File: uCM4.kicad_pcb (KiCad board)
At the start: 2 copper layers, 55 x 40 mm, 39 parts, among them J1 Conn_01x03, J2 Ethernet, J3 Micro_SD_Card, J4 USB_B_Micro, SW1 SW_DIP_x01, SW2 SW_DIP_x01, U1 RT9742GGJ5, U2 74LVC1G07, U3 TPD4EUSB30

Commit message: Bump to version 0.2.0
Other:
- board text added: "µCM4-Net v0.2.0"
- board text removed: "µCM4-Net v0.1.1"
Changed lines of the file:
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@@
   (gr_line (start 175.94 85.04) (end 120.94 125.04) (layer "User.2") (width 0.15))
   (gr_line (start 120.94 88.55) (end 120.94 84.38) (layer "User.2") (width 0.15))
-  (gr_text "µCM4-Net v0.1.1" (at 126.5 111.5 270) (layer "B.SilkS")
+  (gr_text "µCM4-Net v0.2.0" (at 126.5 111.5 270) (layer "B.SilkS")
     (effects (font (size 1 1) (thickness 0.15)) (justify mirror))
   )

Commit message: Add TODOs for planned changes in PCB layout
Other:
- board text added: "TODO: LEDs here"
- board text added: "TODO: SOT-23-5"
- board text added: "TODO: btn here"
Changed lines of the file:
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@@
     (effects (font (size 1 1) (thickness 0.15)))
+  )
+  (gr_text "TODO: LEDs here" (at 172.37 117.11) (layer "User.4")
+    (effects (font (size 0.5 0.5) (thickness 0.125)))
+  )
+  (gr_text "TODO: SOT-23-5" (at 158.71 91.8) (layer "User.4")
+    (effects (font (size 0.5 0.5) (thickness 0.125)))
+  )
+  (gr_text "TODO: btn here" (at 172.55 94.2) (layer "User.4")
+    (effects (font (size 0.5 0.5) (thickness 0.125)))
   )
   (segment (start 139.777771 104.500012) (end 145.620012 104.500012) (width 0.13) (layer "F.Cu") (net 3))

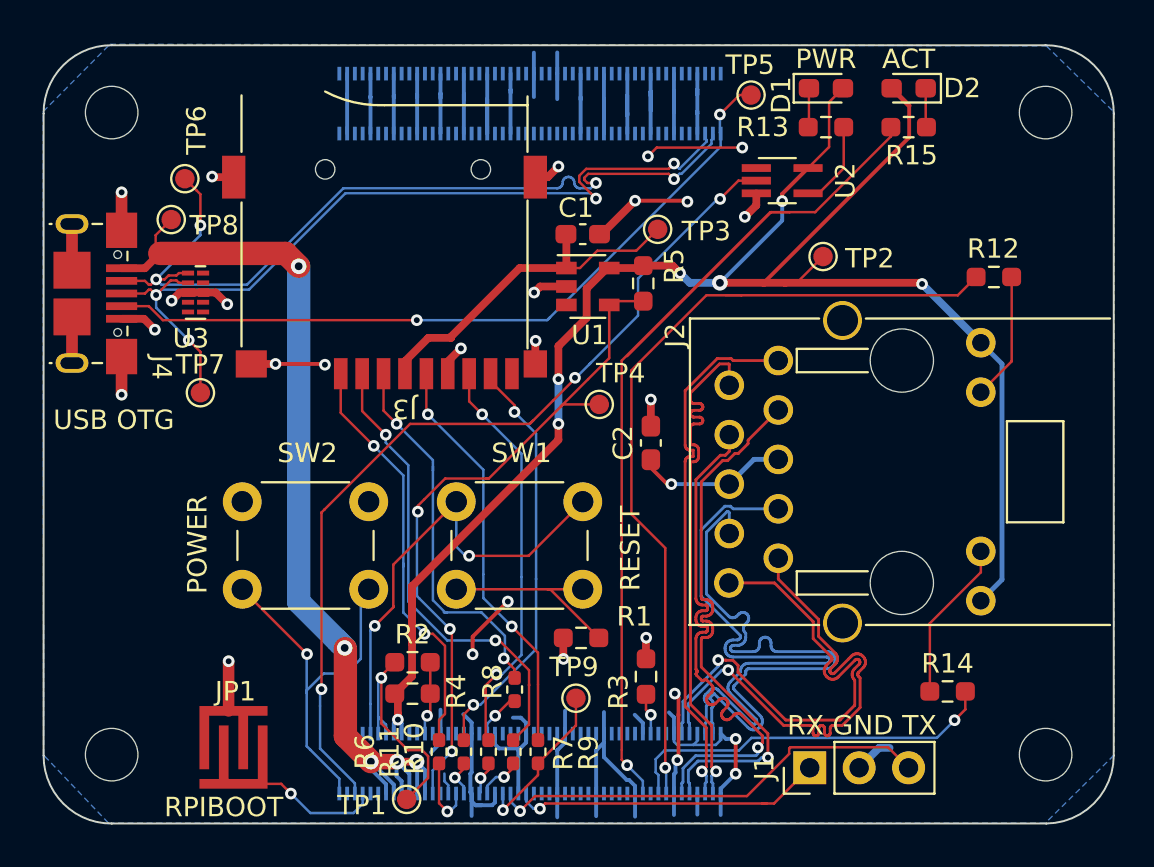
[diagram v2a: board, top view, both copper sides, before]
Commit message: Make preparations for required changes in 0.2.0
Following has been performed and could not be made separately:
- move LEDs to smaller space next to Ethernet
- move buttons to bigger space next to Ethernet
- two changes above makes together handy interface for whole board,
  where almost everything needed is on one side
- move all parts belonging to LEDs and buttons near their new locations
- change footprint of buffer chip to SOT-23-5, which is more likely to
  be used in this version
- reroute traces for all moved parts and do some small adjustments in
  other traces for easier routing (buttons not completed yet!)
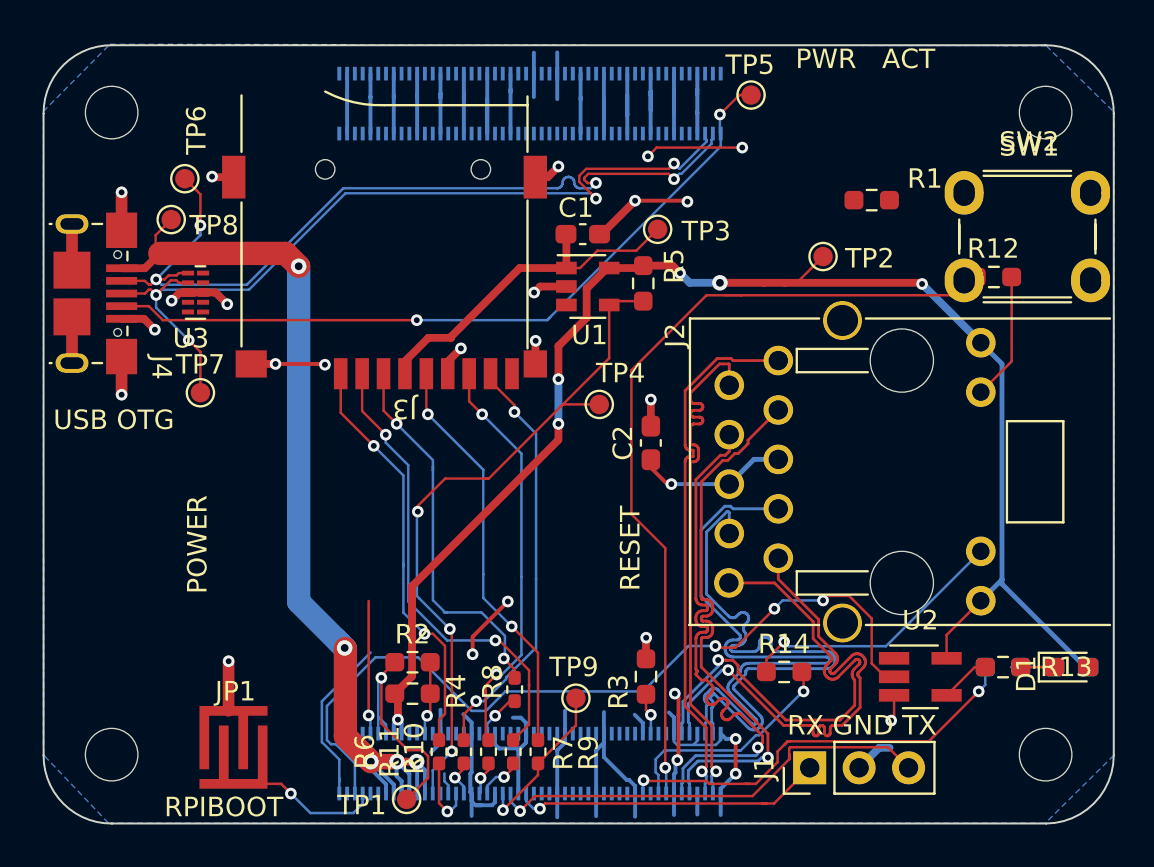
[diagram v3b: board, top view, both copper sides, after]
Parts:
- D2, R15: moved to B.Cu
- U2: footprint Package_TO_SOT_SMD:SOT-353_SC-70-5_Handsoldering -> Package_TO_SOT_SMD:SOT-23-5_HandSoldering
- moved SW2 40.4 mm to (168.2, 92.5)
- moved D1 32.3 mm to (173.8, 117.0)
- moved D2 30.9 mm to (173.8, 117.0), turned to 0 degrees
- moved SW1 30.5 mm to (174.8, 97.2)
- moved R13 29.2 mm to (170.2, 117.0), turned to 0 degrees
- moved R15 28.2 mm to (170.2, 117.0)
- moved R1 27.0 mm to (163.5, 93.0)
- moved U2 26.5 mm to (166.0, 117.5)
- moved R14 8.46 mm to (159.0, 117.2)
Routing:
- net Net-(Module1-Pad21): track 53.2 -> 22.3 mm, vias 1 -> 2
- net /RESET: track 23.9 -> 6.86 mm, vias 2 -> 1
- net +3V3: track 96.3 -> 80.4 mm, vias 7 -> 6
- net /PowerOn: track 19.9 -> 8.78 mm, vias 1 -> 0
- net Net-(R1-Pad1): track 10.2 -> 0.00 mm
- net Net-(Module1-Pad17): track 19.7 -> 11.9 mm
- net Net-(J2-PadL3): track 8.29 -> 14.2 mm, vias 0 -> 1
- net /nPWR_LED: track 46.1 -> 41.9 mm
- net /nPWR_LED_Buffered: track 4.48 -> 2.59 mm
- net GND: track 160.3 -> 159.2 mm, vias 27 -> 26

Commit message: Remove TODOs
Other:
- board text removed: "TODO: LEDs here"
- board text removed: "TODO: SOT-23-5"
- board text removed: "TODO: btn here"
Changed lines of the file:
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@@
     (effects (font (size 1 1) (thickness 0.15)))
-  )
-  (gr_text "TODO: LEDs here" (at 172.37 117.11) (layer "User.4")
-    (effects (font (size 0.5 0.5) (thickness 0.125)))
-  )
-  (gr_text "TODO: SOT-23-5" (at 165.25 117.5) (layer "User.4")
-    (effects (font (size 0.5 0.5) (thickness 0.125)))
-  )
-  (gr_text "TODO: btn here" (at 172.55 94.2) (layer "User.4")
-    (effects (font (size 0.5 0.5) (thickness 0.125)))
   )
   (segment (start 164.195 117.5) (end 163.5 116.805) (width 0.13) (layer "F.Cu") (net 3))

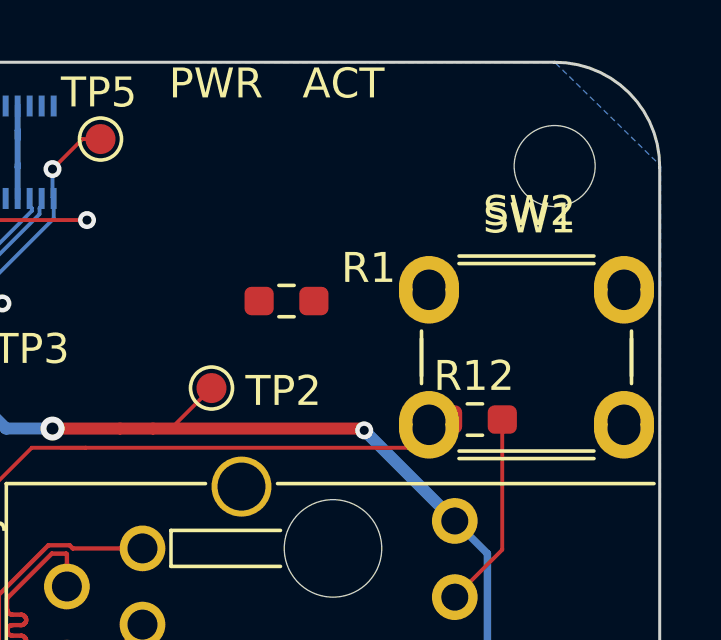
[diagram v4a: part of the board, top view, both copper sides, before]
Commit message: Update footprint for buttons
Now should point to almost finished PTS840.
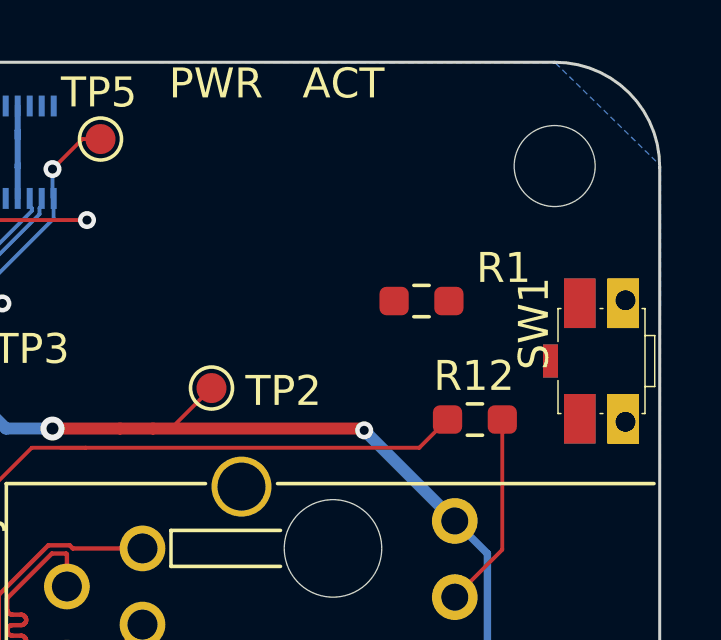
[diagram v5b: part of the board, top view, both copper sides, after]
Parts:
- SW1: footprint Button_Switch_THT:SW_PUSH_6mm -> KiCAD_Randoms:PTS840_PM_SMTR_LFS
- SW2: footprint Button_Switch_THT:SW_PUSH_6mm -> KiCAD_Randoms:PTS840_PM_SMTR_LFS; moved to B.Cu
- moved SW2 6.27 mm to (174.0, 95.0), turned to -90 degrees
- moved R1 4.50 mm to (168.0, 93.0)
- moved SW1 2.37 mm to (174.0, 95.0), turned to 90 degrees

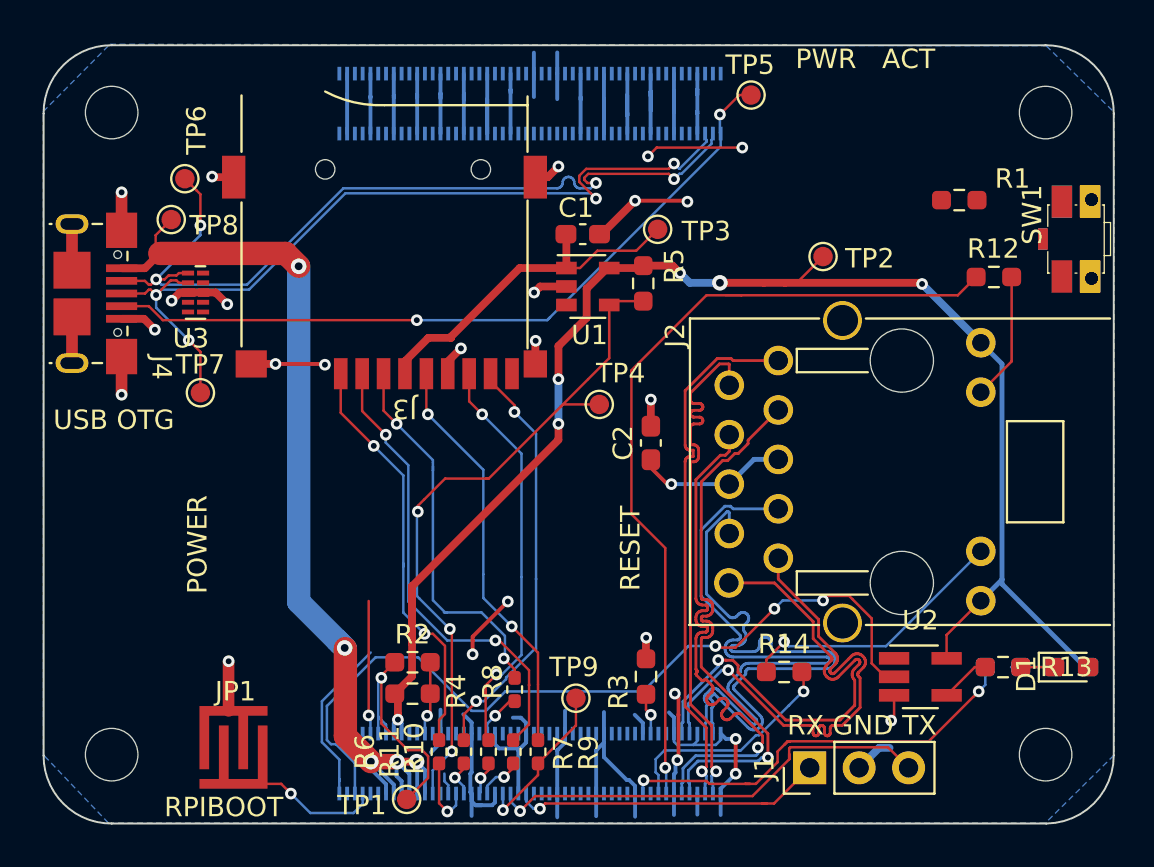
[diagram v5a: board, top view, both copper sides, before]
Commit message: Power buttons - issue #7
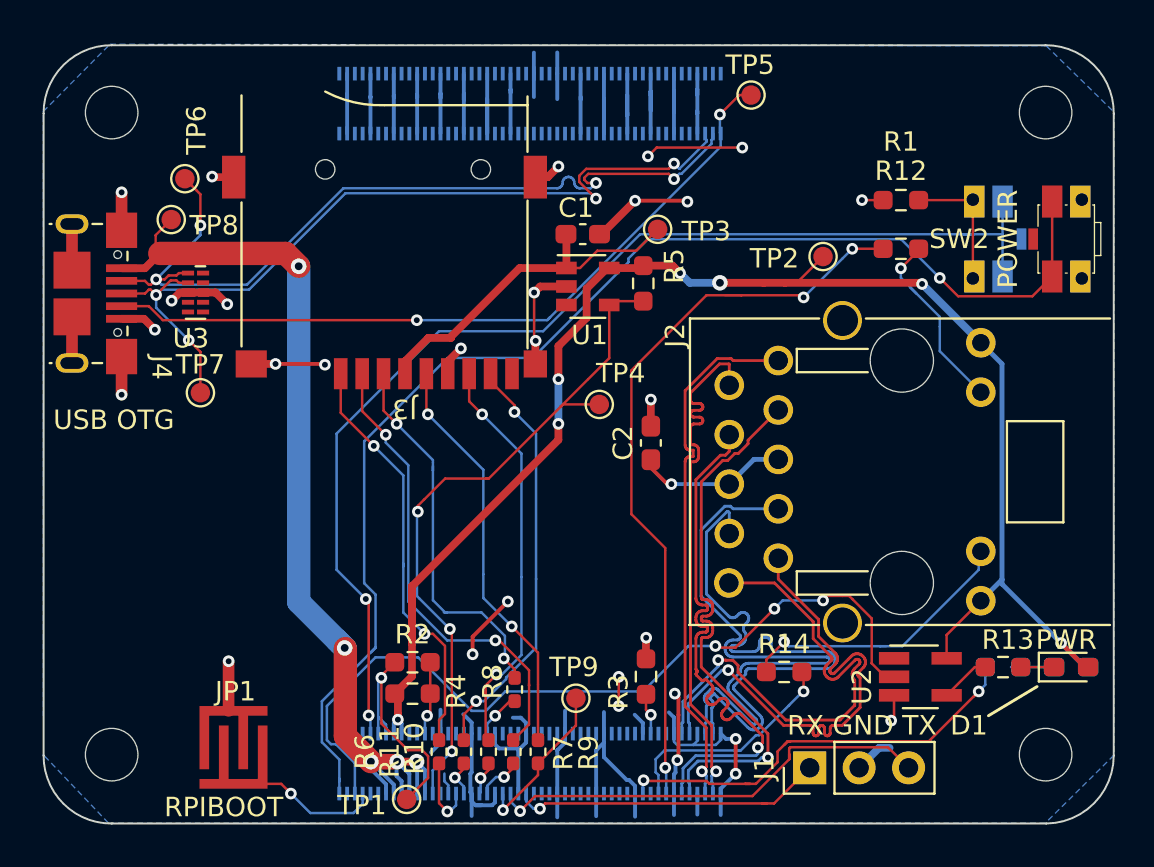
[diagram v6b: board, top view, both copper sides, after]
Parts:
- SW1: moved to B.Cu
- SW2: moved to F.Cu
- moved R12 5.00 mm to (165.0, 95.5)
- moved SW1 4.50 mm to (169.5, 95.0)
- moved R1 3.00 mm to (165.0, 93.0)
- moved SW2 0.50 mm to (173.5, 95.0), turned to 90 degrees
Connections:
- net Net-(Module1-Pad21) renamed /ACT_LED
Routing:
- net /PowerOn: track 8.78 -> 65.7 mm, vias 0 -> 1
- net /RESET: track 6.86 -> 59.0 mm, vias 1 -> 2
- net Net-(R1-Pad1): track 0.00 -> 6.85 mm
- net GND: track 159.2 -> 164.3 mm, vias 26 -> 29
- net Net-(Module1-Pad15): track 43.0 -> 38.9 mm, vias 1 -> 3
- net Net-(J2-PadL2): track 6.74 -> 10.0 mm, vias 0 -> 1
- net +3V3: track 80.4 -> 82.3 mm, vias 6 -> 7
- net Net-(J2-PadL3): track 14.2 -> 14.9 mm

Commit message: Some small adjustments
Nothing important.
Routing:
- net GND: track 164.3 -> 161.7 mm
- net /RESET: track 59.0 -> 61.1 mm
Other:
- board text added: "TODO: 5V TP?"
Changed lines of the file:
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@@
       (effects (font (size 1 1) (thickness 0.15)) (justify mirror))
     )
-    (fp_text user "${REFERENCE}" (at 0.5 1.5 90 unlocked) (layer "B.Fab")
+    (fp_text user "${REFERENCE}" (at 0 4.5 unlocked) (layer "B.Fab")
       (effects (font (size 1 1) (thickness 0.15)) (justify mirror))
     )
@@
     (pad "" smd rect (at 0 1.7 90) (size 1.1 0.5) (layers "B.Cu" "B.Paste" "B.Mask"))
     (pad "1" thru_hole rect (at -2.025 -0.8 90) (locked) (size 1.65 1.05) (drill 0.65 (offset 0.1 0.075)) (layers *.Cu *.Mask)
-      (net 116 "Net-(R1-Pad1)") (pintype "passive"))
+      (net 116 "Net-(R1-Pad1)"))
     (pad "1" thru_hole rect (at 2.025 -0.8 90) (locked) (size 1.65 1.05) (drill 0.65 (offset -0.1 0.075)) (layers *.Cu *.Mask)
-      (net 116 "Net-(R1-Pad1)") (pintype "passive"))
+      (net 116 "Net-(R1-Pad1)"))
     (pad "2" smd rect (at 1.925 0.725 90) (locked) (size 1.65 1.05) (layers "B.Cu" "B.Paste" "B.Mask")
-      (net 164 "/RESET") (pintype "passive"))
+      (net 164 "/RESET"))
     (pad "2" smd rect (at -1.925 0.725 90) (locked) (size 1.65 1.05) (layers "B.Cu" "B.Paste" "B.Mask")
-      (net 164 "/RESET") (pintype "passive"))
+      (net 164 "/RESET"))
   )
   (footprint "Resistor_SMD:R_0603_1608Metric_Pad0.98x0.95mm_HandSolder" (layer "B.Cu")
@@
     (effects (font (size 1 1) (thickness 0.15)))
   )
+  (gr_text "TODO: 5V TP?" (at 132.5 107.5) (layer "User.4")
+    (effects (font (size 0.5 0.5) (thickness 0.125)))
+  )
   (segment (start 164.195 117.5) (end 163.5 116.805) (width 0.13) (layer "F.Cu") (net 3))
   (segment (start 162.5 113.5) (end 162.34002 113.34002) (width 0.13) (layer "F.Cu") (net 3))
@@
   (segment (start 135.962011 120.962011) (end 135.712011 120.962011) (width 0.13) (layer "B.Cu") (net 3))
   (segment (start 136.939 123.5) (end 136.939 121.939) (width 0.13) (layer "B.Cu") (net 3))
-  (segment (start 146.15 97.75) (end 146.15 100.15) (width 0.13) (layer "F.Cu") (net 4))
   (segment (start 128.4 97.75) (end 127.94 97.75) (width 0.4) (layer "F.Cu") (net 4))
   (segment (start 122.4 99) (end 122.4 101.375) (width 0.6) (layer "F.Cu") (net 4))
@@
   (segment (start 164.0875 93) (end 163 93) (width 0.127) (layer "F.Cu") (net 4))
   (segment (start 129.63 91.82) (end 129.6 91.79) (width 0.4) (layer "F.Cu") (net 4))
-  (segment (start 146.15 100.15) (end 146.23 100.23) (width 0.13) (layer "F.Cu") (net 4))
   (segment (start 149.5125 94.75) (end 149.62 94.75) (width 0.4) (layer "F.Cu") (net 4))
   (segment (start 153.57 118.550862) (end 153.382 118.362862) (width 0.2) (layer "F.Cu") (net 4))
@@
   (via (at 137.647 119.485222) (size 0.6) (drill 0.3) (layers "F.Cu" "B.Cu") (net 164))
   (via (at 137.5 113.5) (size 0.6) (drill 0.3) (layers "F.Cu" "B.Cu") (net 164))
+  (segment (start 170.225 96.925) (end 170.225 96.625) (width 0.13) (layer "B.Cu") (net 164))
+  (segment (start 168.844531 94.755469) (end 167.744531 94.755469) (width 0.13) (layer "B.Cu") (net 164))
+  (segment (start 168.355469 94.755469) (end 166.755469 94.755469) (width 0.13) (layer "B.Cu") (net 164))
   (segment (start 141.260511 99.739489) (end 146.610146 99.739489) (width 0.127) (layer "B.Cu") (net 164))
   (segment (start 136 112) (end 136 105) (width 0.13) (layer "B.Cu") (net 164))
+  (segment (start 170.225 96.625) (end 168.355469 94.755469) (width 0.13) (layer "B.Cu") (net 164))
+  (segment (start 166.755469 94.755469) (end 167.744531 94.755469) (width 0.127) (layer "B.Cu") (net 164))
+  (segment (start 151.594166 94.755469) (end 166.755469 94.755469) (width 0.127) (layer "B.Cu") (net 164))
   (segment (start 168.244531 94.755469) (end 168.755469 94.755469) (width 0.127) (layer "B.Cu") (net 164))
-  (segment (start 170.225 93.075) (end 170.225 94.775) (width 0.127) (layer "B.Cu") (net 164))
-  (segment (start 170.205469 94.755469) (end 170.225 94.775) (width 0.127) (layer "B.Cu") (net 164))
   (segment (start 137.739 119.577222) (end 137.647 119.485222) (width 0.13) (layer "B.Cu") (net 164))
-  (segment (start 170.225 94.775) (end 170.225 96.925) (width 0.127) (layer "B.Cu") (net 164))
   (segment (start 137.5 113.5) (end 136 112) (width 0.13) (layer "B.Cu") (net 164))
   (segment (start 146.610146 99.739489) (end 151.594166 94.755469) (width 0.127) (layer "B.Cu") (net 164))
-  (segment (start 168.244531 94.755469) (end 170.205469 94.755469) (width 0.127) (layer "B.Cu") (net 164))
-  (segment (start 151.594166 94.755469) (end 168.244531 94.755469) (width 0.127) (layer "B.Cu") (net 164))
   (segment (start 137.739 120.42) (end 137.739 119.577222) (width 0.13) (layer "B.Cu") (net 164))
+  (segment (start 170.225 93.075) (end 170.225 93.375) (width 0.13) (layer "B.Cu") (net 164))
+  (segment (start 170.225 93.375) (end 168.844531 94.755469) (width 0.13) (layer "B.Cu") (net 164))
   (segment (start 136 105) (end 141.260511 99.739489) (width 0.13) (layer "B.Cu") (net 164))
+  (segment (start 167.744531 94.755469) (end 168.244531 94.755469) (width 0.127) (layer "B.Cu") (net 164))
   (zone (net 0) (net_name "") (layers F&B.Cu) (name "Wireless Cutout") (hatch edge 0.508)
     (connect_pads (clearance 0))

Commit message: Update PCB after schematics changes
Most significantly LCSC# and some part names. Nothing important from PCB
perspective, despite amount of changes.
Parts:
- U2: value 74LVC1G07 -> SN74LVC1G07DBVR
